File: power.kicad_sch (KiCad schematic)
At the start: 43 parts, among them Q1 CSD18511Q5A, Q2 CSD18511Q5A, Q3 CSD18511Q5A, Q4 CSD18511Q5A, U1 LM25119PSQ/NOPB, U2 DS4432U+, U3 INA260

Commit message: added RI pullup resistors for #16. updated BOM. bumped version number to 3
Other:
- title: (none) -> emberOne/00
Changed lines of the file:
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@@
 	(paper "A3")
 	(title_block
-		(date "2024-11-25")
-		(rev "2")
+		(title "emberOne/00")
+		(date "2025-02-25")
+		(rev "3")
 	)
 	(text "I2C Address: 0x40"

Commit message: added ceramic output caps for #26, added SW Node snubbers for #25, added LO and HO resistor pads for #24, reoriented inductors for #23. Changed R_FS/R11 to 39k for #21, updated BM1362 footprint spacing for #18 (might be more to do here)
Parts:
- added C26: 1uF, Capacitor_SMD:C_0805_2012Metric, symbol Device:C
- added C27: 0.1uF, Capacitor_SMD:C_0805_2012Metric, symbol Device:C
- added C28, C29: 4.7nF, Capacitor_SMD:C_0805_2012Metric, symbol Device:C
- added R23, R24, R25, R26: 0, Resistor_SMD:R_0603_1608Metric, symbol Device:R_US
- added R27, R28: 6.8, Resistor_SMD:R_0603_1608Metric, symbol Device:R_US
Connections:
- net GND: now also C26.2, C27.2, R27.2, R28.2
- net SW1: now also L1.2, C28.1; no longer L1.1
- net SW2: now also R9.2, C29.1; no longer R9.1
- net VOUT: now also L1.1, C26.1, C27.1; no longer L1.2
- net at C6.1, U1.19 (RAMP2): now also R9.1; no longer R9.2
- net at Q4.4 (G): now also R25.2; no longer U1.23 (LO2)
- net at Q3.4 (G): now also R26.2; no longer U1.26 (HO2)
- net at U1.2 (LO1): now also R24.1; no longer Q2.4 (G)
- net at U1.31 (HO1): now also R23.1; no longer Q1.4 (G)
- new net: C29.2, R28.1
- new net: Q1.4 (G), R23.2
- new net: C28.2, R27.1
- new net: R26.1, U1.26 (HO2)
- new net: R25.1, U1.23 (LO2)
- new net: Q2.4 (G), R24.2
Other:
- moved on the sheet: C1, C10, C11, C12, C13, C14, C15, C16, C17, C18, C2, C3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

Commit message: tightened up the SW loops a bit in layout
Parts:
- R11: value 80.6k -> 39k; DK 311-80.6KLRCT-ND -> (none); PARTNO RC0402FR-0780K6L -> (none)
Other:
- note added: "R_FS"
- moved on the sheet: C1, C10, C11, C12, C13, C14, C15, C16, C17, C18, C2, C26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

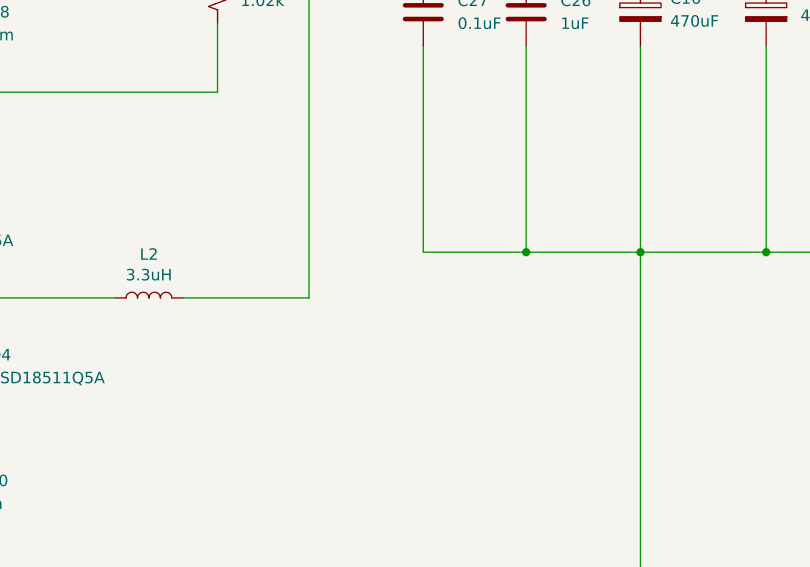
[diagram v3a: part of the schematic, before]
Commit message: added SMA VDD test port. Switched to 6 layers and doubled up power tracks.
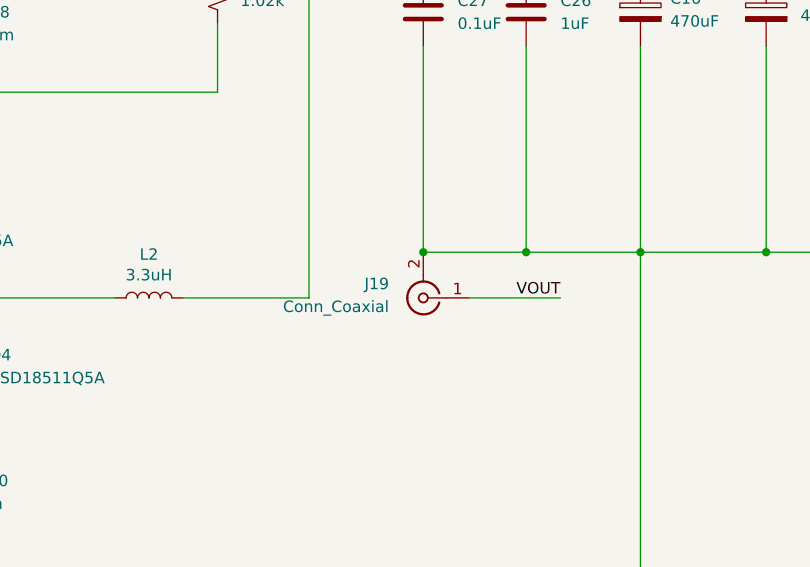
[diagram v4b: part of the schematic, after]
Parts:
- added J19: Conn_Coaxial, emberone:LINX_CONSMA001-SMD-G, symbol Connector:Conn_Coaxial
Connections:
- net GND: now also J19.2 (Ext)
- net VOUT: now also J19.1 (In)
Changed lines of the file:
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@@
 	)
 	(junction
+		(at 344.17 121.92)
+		(diameter 0)
+		(color 0 0 0 0)
+	)
+	(junction
 		(at 160.02 171.45)
 		(diameter 0)
@@
 	(wire
 		(pts
+			(xy 349.25 127) (xy 359.41 127)
+		)
+		(stroke
+			(width 0)
+			(type default)
+		)
+	)
+	(wire
+		(pts
 			(xy 213.36 129.54) (xy 213.36 114.3)
 		)
@@
 		)
 	)
+	(label "VOUT"
+		(at 359.41 127 180)
+		(effects
+			(font
+				(size 1.27 1.27)
+			)
+			(justify right bottom)
+		)
+	)
 	(label "3V3"
 		(at 261.62 201.93 0)
@@
 					(unit 1)
 				)
+			)
+		)
+	)
+	(symbol
+		(lib_id "Connector:Conn_Coaxial")
+		(at 344.17 127 180)
+		(unit 1)
+		(exclude_from_sim no)
+		(in_bom yes)
+		(on_board yes)
+		(dnp no)
+		(fields_autoplaced yes)
+		(property "Reference" "J19"
+			(at 340.36 125.4367 0)
+			(effects
+				(font
+					(size 1.27 1.27)
+				)
+				(justify left)
+			)
+		)
+		(property "Value" "Conn_Coaxial"
+			(at 340.36 127.9767 0)
+			(effects
+				(font
+					(size 1.27 1.27)
+				)
+				(justify left)
+			)
+		)
+		(property "Footprint" "emberone:LINX_CONSMA001-SMD-G"
+			(at 344.17 127 0)
+			(effects
+				(font
+					(size 1.27 1.27)
+				)
+				(hide yes)
+			)
+		)
+		(property "Datasheet" "~"
+			(at 344.17 127 0)
+			(effects
+				(font
+					(size 1.27 1.27)
+				)
+				(hide yes)
+			)
+		)
+		(property "Description" "coaxial connector (BNC, SMA, SMB, SMC, Cinch/RCA, LEMO, ...)"
+			(at 344.17 127 0)
+			(effects
+				(font
+					(size 1.27 1.27)
+				)
+				(hide yes)
+			)
+		)
+		(property "PARTNO" "CONSMA001-SMD-G"
+			(at 344.17 127 0)
+			(effects
+				(font
+					(size 1.27 1.27)
+				)
+				(hide yes)
+			)
+		)
+		(property "DK" "CONSMA001-SMD-G-ND"
+			(at 344.17 127 0)
+			(effects
+				(font
+					(size 1.27 1.27)
+				)
+				(hide yes)
+			)
+		)
+		(pin "1"
+		)
+		(pin "2"
+		)
+		(instances
+			(project ""
+				(path "/b036224c-4cdf-48cc-81df-19bc5283ebd2/77c510ef-c2c8-433b-9442-e0d7684769dc"
+					(reference "J19")
+					(unit 1)
+				)

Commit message: switched big SMA for a smaller MMCX connector
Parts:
- J19: footprint emberone:LINX_CONSMA001-SMD-G -> emberone:SAMTEC_MMCX-P-P-H-ST-TH1; DK CONSMA001-SMD-G-ND -> SAM10618-ND; PARTNO CONSMA001-SMD-G -> MMCX-P-P-H-ST-TH1
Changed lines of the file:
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@@
 			)
 		)
-		(property "Footprint" "emberone:LINX_CONSMA001-SMD-G"
+		(property "Footprint" "emberone:SAMTEC_MMCX-P-P-H-ST-TH1"
 			(at 344.17 127 0)
 			(effects
@@
 			)
 		)
-		(property "Description" "coaxial connector (BNC, SMA, SMB, SMC, Cinch/RCA, LEMO, ...)"
+		(property "Description" ""
 			(at 344.17 127 0)
 			(effects
@@
 			)
 		)
-		(property "PARTNO" "CONSMA001-SMD-G"
+		(property "PARTNO" "MMCX-P-P-H-ST-TH1"
 			(at 344.17 127 0)
 			(effects
@@
 			)
 		)
-		(property "DK" "CONSMA001-SMD-G-ND"
+		(property "DK" "SAM10618-ND"
 			(at 344.17 127 0)
 			(effects

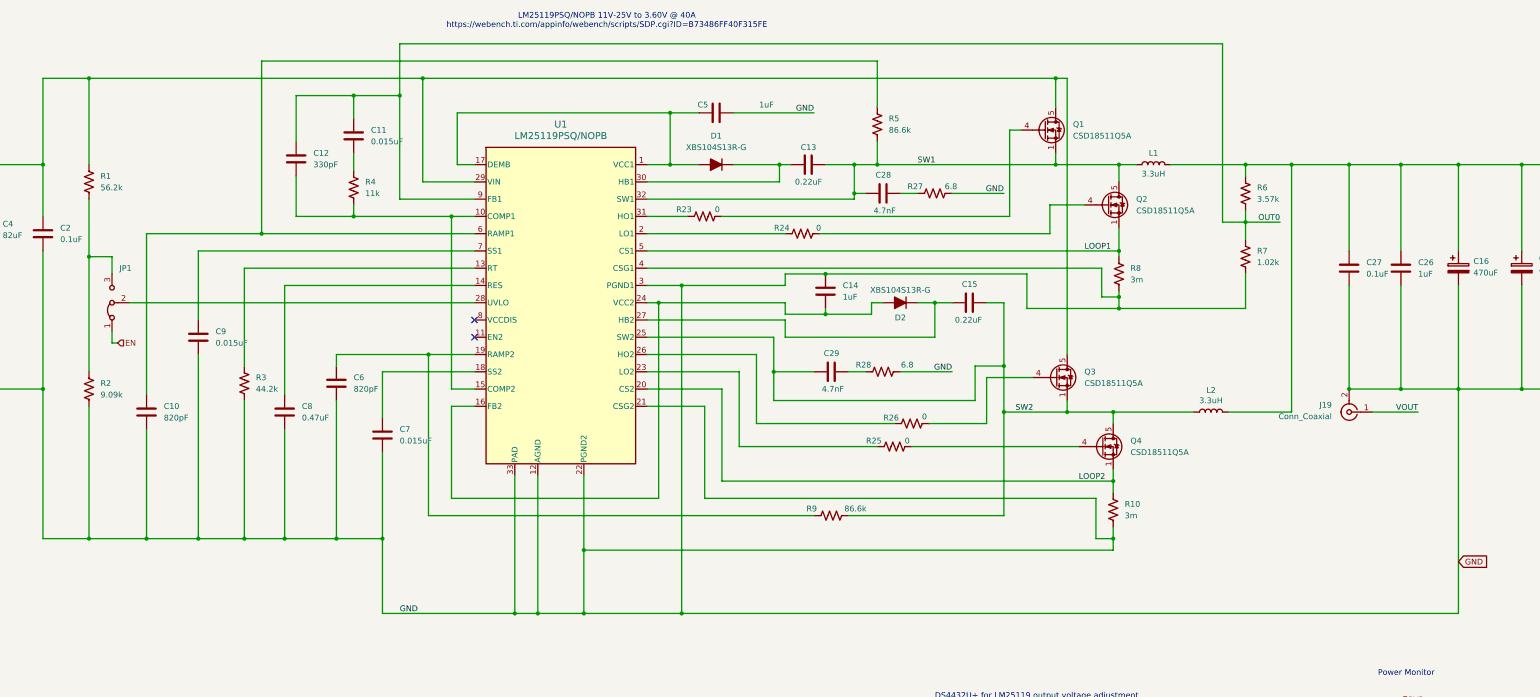
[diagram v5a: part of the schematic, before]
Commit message: added LM25119-datasheet recommended filter on CSx/CSGx pins
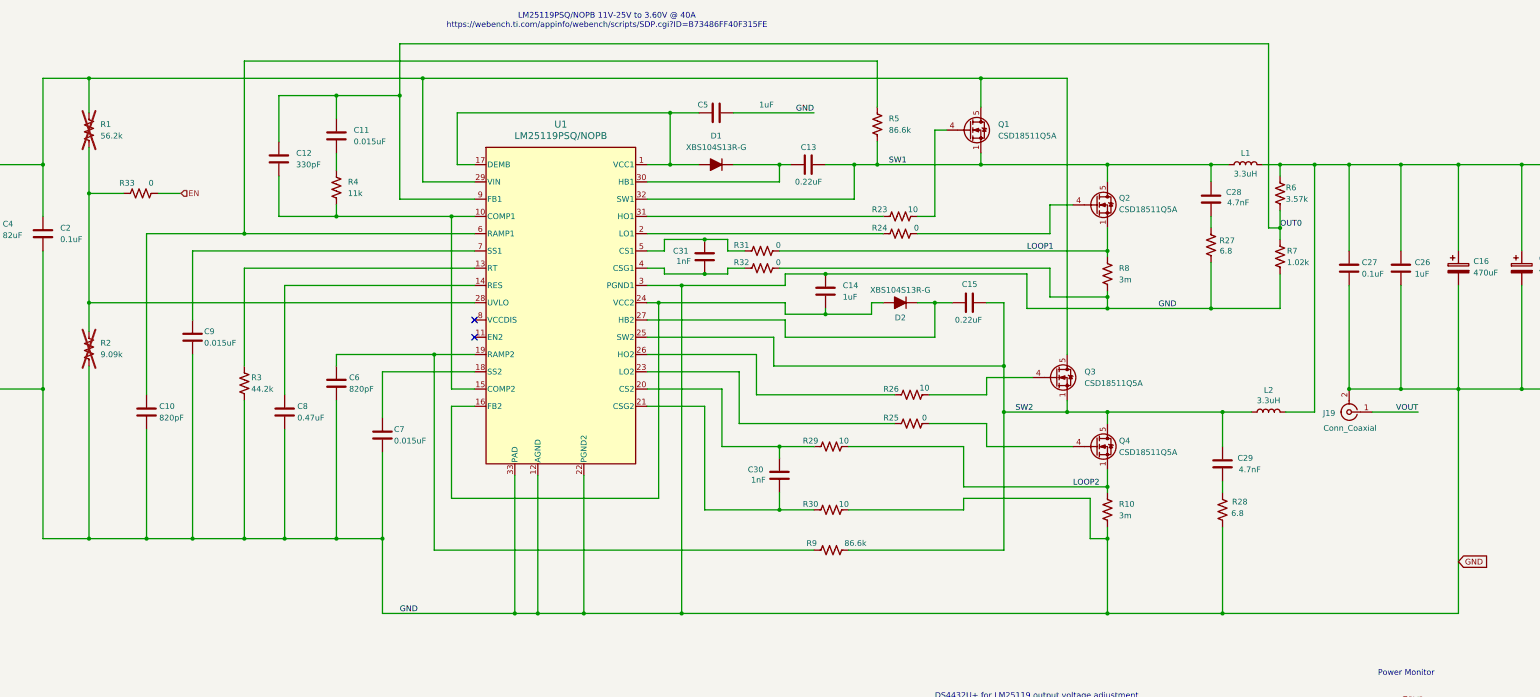
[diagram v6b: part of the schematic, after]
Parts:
- removed JP1: Jumper_3_Bridged12, Jumper:SolderJumper-3_P1.3mm_Bridged12_Pad1.0x1.5mm, symbol Jumper:Jumper_3_Bridged12
- added C30, C31: 1nF, Capacitor_SMD:C_0805_2012Metric, symbol Device:C
- added R29, R30: 10, Resistor_SMD:R_0603_1608Metric, symbol Device:R_US
- added R31, R32, R33: 0, Resistor_SMD:R_0603_1608Metric, symbol Device:R_US
- C28, C29: DK 1276-2947-1-ND -> (none); PARTNO CL21B224KBFNFNE -> (none)
- R1, R2: now not fitted; now left out of the parts list
- R23, R26: value 0 -> 10
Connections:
- net EN: now also R33.1
- net GND: now also R30.2, R32.2; no longer U1.21 (CSG2), U1.4 (CSG1)
- net LOOP1: now also R31.2; no longer U1.5 (CS1)
- net LOOP2: now also R29.2; no longer U1.20 (CS2)
- net at R1.2, R2.1: now also U1.28 (UVLO), R33.2
- new net: C30.2, R29.1, U1.20 (CS2)
- new net: C31.2, R31.1, U1.5 (CS1)
- new net: C31.1, R32.1, U1.4 (CSG1)
- new net: C30.1, R30.1, U1.21 (CSG2)
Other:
- moved on the sheet: C11, C12, C28, C29, C9, L1, L2, Q1, Q2, Q4, R10, R23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
